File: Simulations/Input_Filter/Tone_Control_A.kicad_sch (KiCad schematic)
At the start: 11 parts, among them U17 TL072

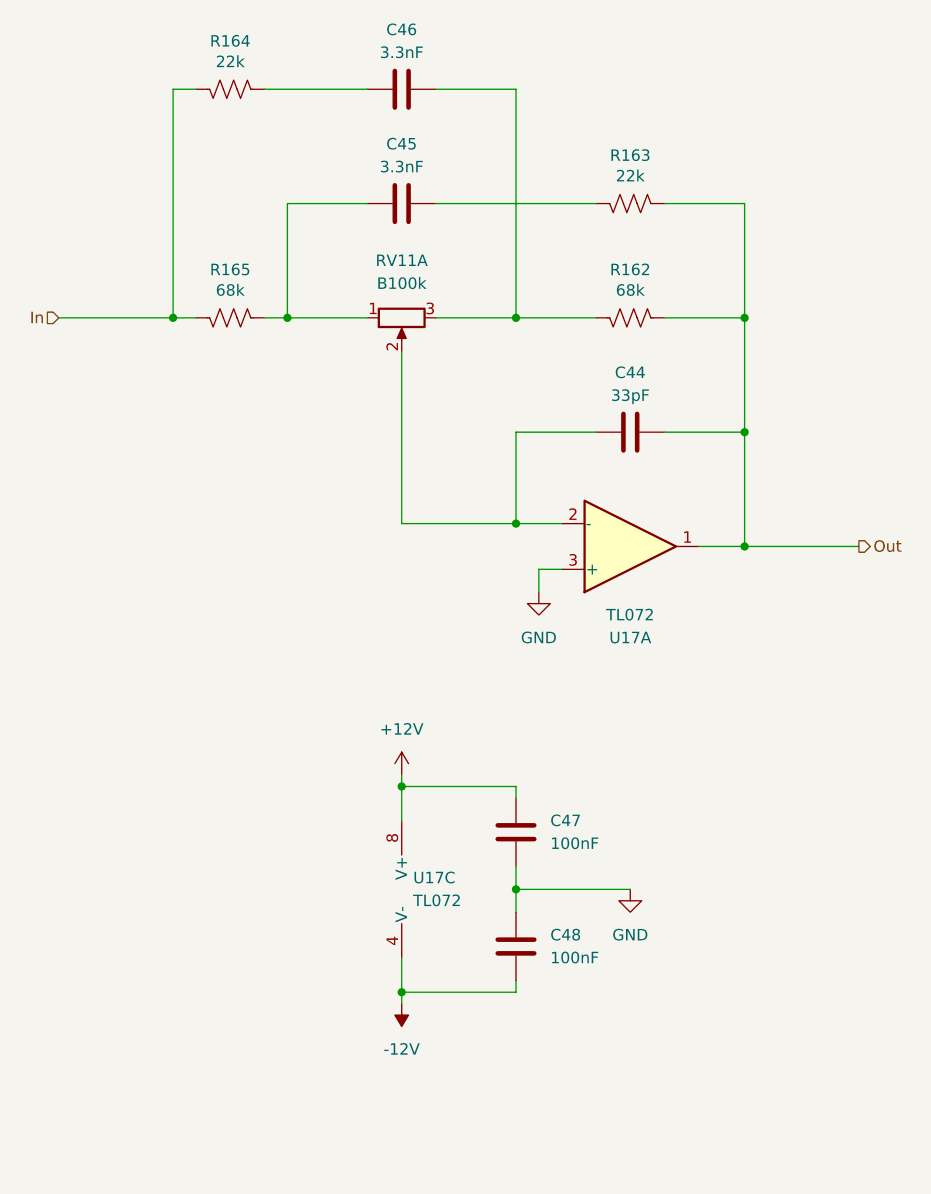
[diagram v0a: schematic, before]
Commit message: Scaled up components in Tone Control part
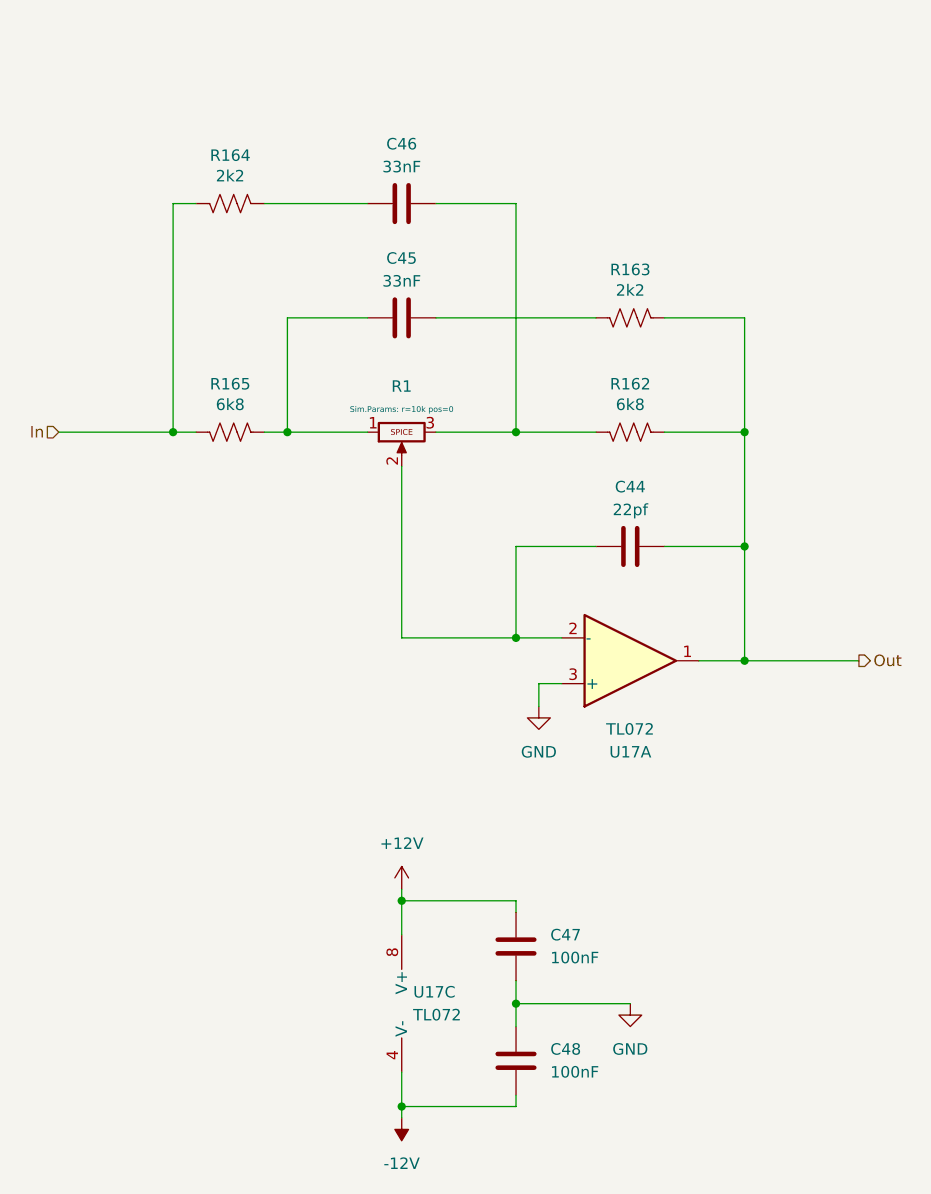
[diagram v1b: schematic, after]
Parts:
- removed RV11: B100k, Potentiometer_THT:Potentiometer_Alps_RK09L_Double_Vertical, symbol Device:R_Potentiometer_Dual_Separate
- added R1: Potentiometer, symbol Simulation_SPICE:Potentiometer
- C44: value 33pF -> 22pf
- C45, C46: value 3.3nF -> 33nF
- R162, R165: value 68k -> 6k8
- R163, R164: value 22k -> 2k2
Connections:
- net at C44.1, U17.2 (-): now also R1.2
- net at C45.1, R165.2: now also R1.1
- net at C46.2, R162.1: now also R1.3
